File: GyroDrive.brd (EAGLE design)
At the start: 8.1 x 21 mm, 35 parts, among them Q1 TF412ST5G, Q2 TF412ST5G, Q3 TF412ST5G, Q4 TF412ST5G, Q5 TF412ST5G, Q6 TF412ST5G

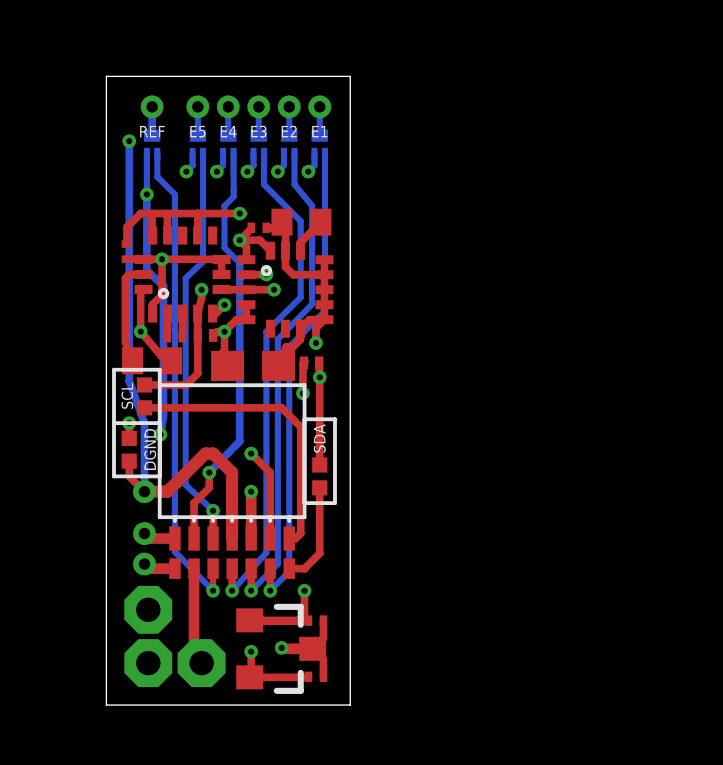
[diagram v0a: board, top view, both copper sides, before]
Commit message: Rev 2 submitted to Advanced Circuits for quote. Fixed spacing issues.
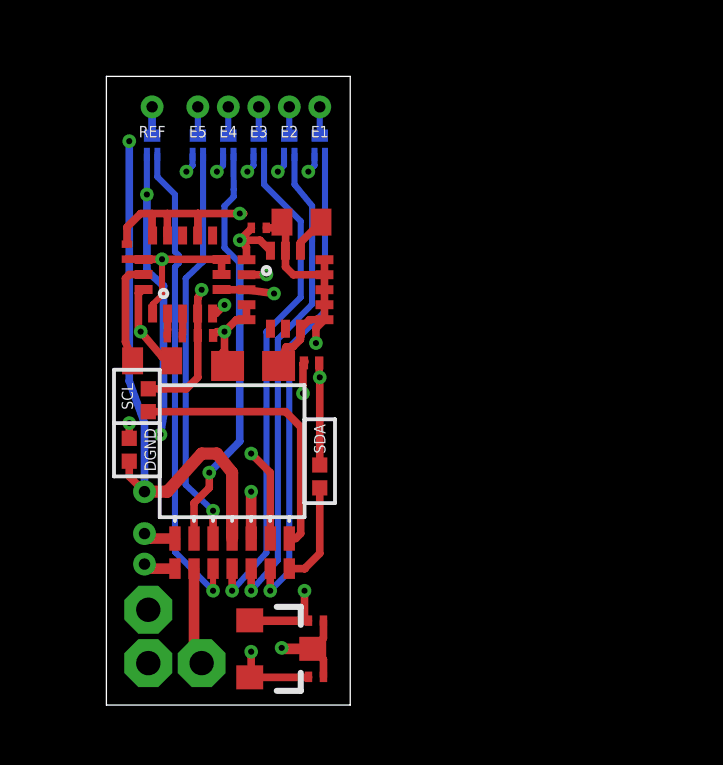
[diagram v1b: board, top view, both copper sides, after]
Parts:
- moved J_SCL 0.18 mm to (1.40, 10.2)

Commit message: Changed schematic to make more sense (Rev 3 to Advanced Circuits)
- Changed input voltage net name from +15V to VCC because VCC can be anything from 2.5V to 30V

- Separate nets for digital and analog grounds (DGND and GND)
-- Causes DRC to catch my mistake when digital and analog ground overlap

- New nets SDAOUT and SCLOUT to represent SDA and SCL after passing through jumper
-- Stops ratsnest from telling me I have things to do when the two terminals of the jumper are not connected to each other
-- Pullup resistors moved to SDA and SCL nets (they used to be near omnetics connector on schematic, which put them on SDAOUT and SCLOUT)

- Capacitors renumbered and moved around
-- Location on schematic is now more representative of location on the board
-- Numbered so that capacitors that are associated with the same IC are sequential.
--- C1-C2 for regulator
--- C3 for big bypass capacitor
--- C4-C5 for L3GD20H
--- C6-C8 for LSM303D
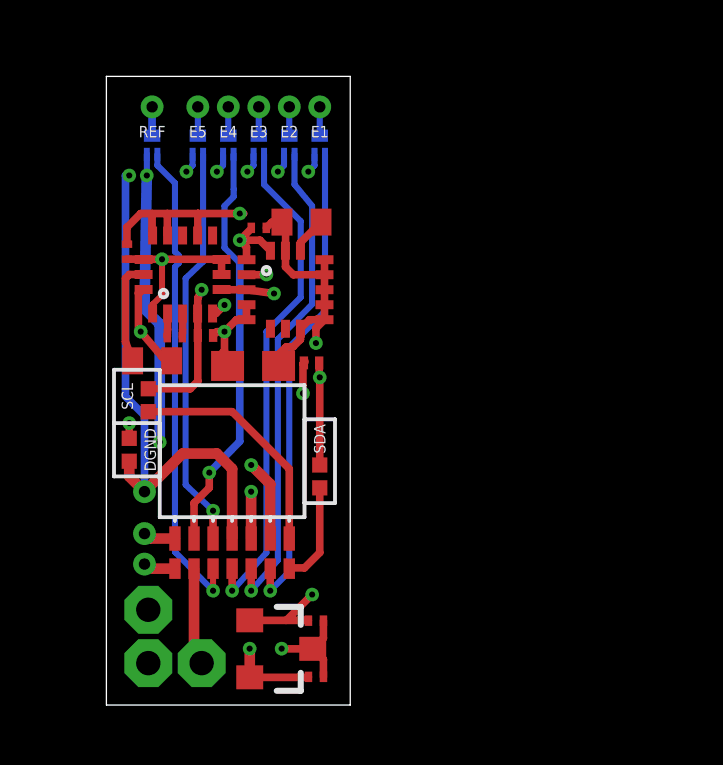
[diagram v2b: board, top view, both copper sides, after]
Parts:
- removed C9: 0.22 uF, resistor:C0201
- added C6: 0.1uF, resistor:C0201
- C3: value 0.1uF -> 10uF; device resistor:C0201 -> resistor:C0603
- C5: value 10uF -> 0.01 uF; device resistor:C0603 -> resistor:C0402
- C7: value 0.01 uF -> 0.22 uF; device resistor:C0402 -> resistor:C0201
- moved C7 5.70 mm to (2.28, 12.3)
- moved C3 5.67 mm to (4.89, 11.3), turned to 0 degrees
- moved C5 5.06 mm to (6.50, 16.1), turned to 180 degrees
- turned J_GND to 270 degrees
- turned J_SCL to 270 degrees
- turned J_SDA to 270 degrees
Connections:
- net +15V renamed VCC
- net N$11 renamed STIM1OUT
- net N$12 renamed ICOM
- net N$15 renamed IX
- net N$16 renamed STIM1IN
- new net DGND: C1.2, C2.2, C3.2, C4.2, C5.2, C6.2, C8.2, J_GND.1, U$1.P$10, U$1.P$11, U$1.P$12, U$1.P$13, U$1.P$15, U$1.P$8, U$1.P$9, U$2.3, U$3.P$10, U$3.P$12, U$3.P$13, U$3.P$16, U$3.P$5
- new net SCLOUT: J_SCL.2, U$10.K
- new net SDAOUT: J_SDA.2, U$10.P
- net +3V3: now also C6.1; no longer C5.1
- net GND: no longer C1.2, C2.2, C3.2, C4.2, C5.2, C7.2, C8.2, J_GND.1, U$1.P$10, U$1.P$11, U$1.P$12, U$1.P$13, U$1.P$15, U$1.P$8, U$1.P$9, U$2.3, U$3.P$10, U$3.P$12, U$3.P$13, U$3.P$16, U$3.P$5
- net N$2: now also C7.1; no longer C9.1
- net N$3: now also C7.2; no longer C9.2
- net N$9: now also C5.1; no longer C7.1
- net SCL: no longer J_SCL.2, U$10.K
- net SDA: no longer J_SDA.2, U$10.P
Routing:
- net GND: track 49.7 -> 23.0 mm, vias 7 -> 1
- net DGND: track 0.00 -> 24.8 mm, vias 0 -> 6
- net SCL: track 17.1 -> 7.74 mm
- net SCLOUT: track 0.00 -> 7.81 mm
- net SDA: track 13.8 -> 10.4 mm
- net SDAOUT: track 0.00 -> 3.40 mm
- net VCC: track 30.9 -> 30.3 mm
- net +3V3: track 25.4 -> 24.8 mm
- added copper zone on layer 3, net DGND

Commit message: WIP: reroute with no vias or traces under chip
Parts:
- moved C7 13.8 mm to (15.7, 9.21)
- moved U$3 13.8 mm to (16.0, 11.3)
- moved C6 13.6 mm to (14.0, 12.6)
- moved R1 13.0 mm to (15.7, 8.51), turned to 180 degrees
- moved C8 11.6 mm to (13.1, 12.0), turned to 90 degrees
- moved R2 11.3 mm to (17.8, 14.4)
- moved C5 11.3 mm to (17.7, 17.7), turned to 270 degrees
- moved C4 10.0 mm to (14.8, 18.6), turned to 90 degrees
- moved U$1 9.64 mm to (15.2, 16.5)
- moved C3 8.55 mm to (13.2, 9.33), turned to 90 degrees
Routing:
- net VCC: track 30.3 -> 0.00 mm, vias 9 -> 0
- net GND: track 23.0 -> 4.73 mm, vias 1 -> 0
- net S3: track 16.7 -> 0.00 mm, vias 1 -> 0
- net S2: track 16.3 -> 0.00 mm, vias 1 -> 0
- net VGND: track 16.2 -> 0.00 mm, vias 1 -> 0
- net S1: track 16.0 -> 0.00 mm, vias 1 -> 0
- net S4: track 13.8 -> 0.00 mm, vias 1 -> 0
- net S5: track 13.5 -> 0.00 mm, vias 1 -> 0
- net SCL: track 7.74 -> 18.1 mm, vias 2 -> 0
- net SCLOUT: track 7.81 -> 0.00 mm
- net SDA: track 10.4 -> 16.5 mm, vias 2 -> 0
- net +3V3: track 24.8 -> 18.9 mm, vias 5 -> 4
- net SDAOUT: track 3.40 -> 0.00 mm
- net DGND: track 24.8 -> 27.2 mm, vias 6 -> 3
- net N$1: track 3.45 -> 1.60 mm
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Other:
- board size 8.1 x 21 mm -> 8.3 x 21 mm

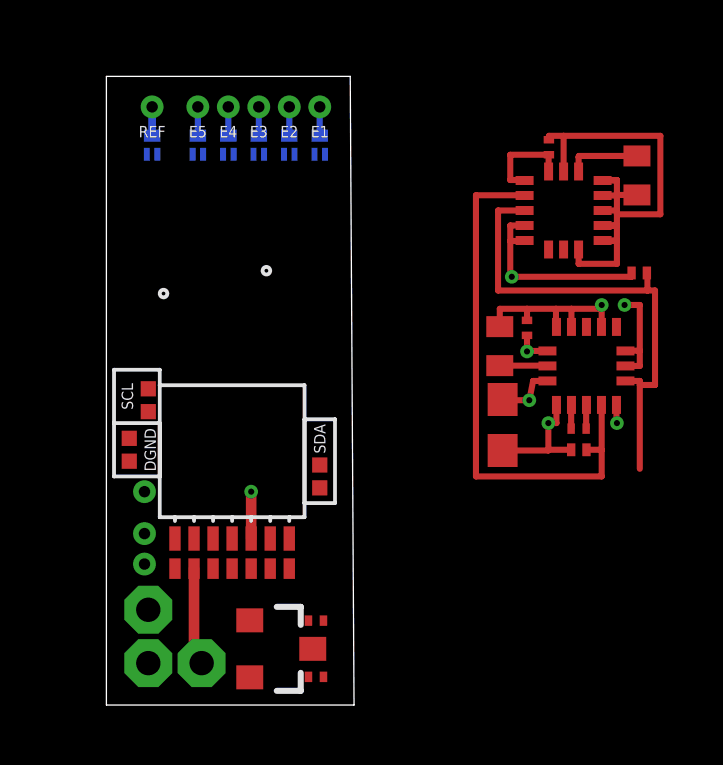
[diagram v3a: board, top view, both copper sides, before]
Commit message: Switched to Invensense MPU-9250
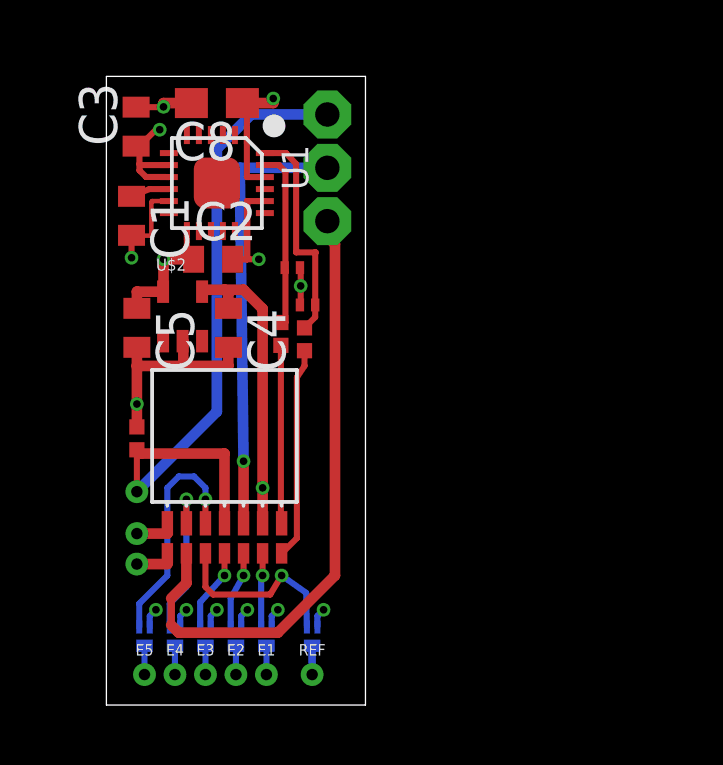
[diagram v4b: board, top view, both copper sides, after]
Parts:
- removed C6: 0.1uF, resistor:C0201
- removed C7: 0.22 uF, resistor:C0201
- removed U$1: L3GD20H, st:LGA16L
- removed U$3: LSM303D, st:LGA16L
- added U1: (no value), Grove - IMU 10DOF v1.1:LEAD-QFN24
- C1, C2: device resistor:C0201 -> resistor:C0402
- C3: value 10uF -> 10nF; device resistor:C0603 -> resistor:C0402
- C4: value 0.1uF -> (none); device resistor:C0201 -> resistor:C0402
- C5: value 0.01 uF -> (none)
- C8: value 4.7uF -> (none); device resistor:C0402 -> resistor:C0603
- U$2: value LM3480IM4 -> 2.5V; device SparkFun-PowerIC:SOT23-3 -> michael-stetner:SC70
- moved REF 19.7 mm to (6.86, 1.02), turned to 180 degrees
- moved E1 19.0 mm to (5.33, 1.02), turned to 180 degrees
- moved E2 19.0 mm to (4.32, 1.02), turned to 180 degrees
- moved E3 19.0 mm to (3.30, 1.02), turned to 180 degrees
- moved E4 19.0 mm to (2.29, 1.02), turned to 180 degrees
- moved E5 19.0 mm to (1.27, 1.02), turned to 180 degrees
- moved ICOM 17.6 mm to (7.37, 17.9)
- moved MOTORGND 17.6 mm to (7.37, 19.7)
- moved C5 17.4 mm to (1.02, 12.6)
- moved Q6 17.2 mm to (6.86, 2.29), turned to 270 degrees
- moved C1 16.6 mm to (0.84, 16.3), turned to 270 degrees
- moved Q1 16.5 mm to (5.33, 2.29), turned to 270 degrees
- moved Q2 16.5 mm to (4.32, 2.29), turned to 270 degrees
- moved Q3 16.5 mm to (3.30, 2.29), turned to 270 degrees
- moved Q4 16.5 mm to (2.29, 2.29), turned to 270 degrees
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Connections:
- removed net +3V3: C2.1, C3.1, C4.1, C6.1, R1.2, R2.2, U$1.P$1, U$1.P$16, U$1.P$4, U$1.P$5, U$2.1, U$3.P$1, U$3.P$14, U$3.P$7, U$3.P$8
- removed net N$1: C8.1, U$3.P$15
- removed net N$3: C7.2, U$3.P$2
- removed net N$9: C5.1, U$1.P$14
- new net VDD: C2.1, C3.1, C5.1, C8.1, R1.2, R2.2, U$2.5, U1.1, U1.13, U1.22, U1.8, U1.9
- net DGND: now also U$2.2, U1.11, U1.18, U1.20; no longer C6.2, U$1.P$10, U$1.P$11, U$1.P$12, U$1.P$13, U$1.P$15, U$1.P$8, U$1.P$9, U$2.3, U$3.P$10, U$3.P$12, U$3.P$13, U$3.P$16, U$3.P$5
- net N$2: now also C1.1, U1.10; no longer C7.1, U$3.P$3
- net SCL: now also U1.23; no longer U$1.P$2, U$3.P$4
- net SDA: now also U1.24; no longer U$1.P$3, U$3.P$6
- net VCC: now also C4.1, U$2.4; no longer C1.1, U$2.2
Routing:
- net +3V3: track 18.9 -> 0.00 mm, vias 4 -> 0
- net GND: track 4.73 -> 23.4 mm
- net IX: track 3.25 -> 20.9 mm
- net VCC: track 0.00 -> 15.3 mm, vias 0 -> 7
- net VDD: track 0.00 -> 14.8 mm, vias 0 -> 4
- net SCL: track 18.1 -> 6.09 mm
- net DGND: track 27.2 -> 18.1 mm, vias 3 -> 4
- net SDA: track 16.5 -> 7.47 mm
- net S5: track 0.00 -> 7.80 mm, vias 0 -> 1
- net SDAOUT: track 0.00 -> 7.04 mm
- net VGND: track 0.00 -> 6.27 mm, vias 0 -> 1
- net SCLOUT: track 0.00 -> 5.94 mm
- net S4: track 0.00 -> 5.29 mm, vias 0 -> 1
- net ICOM: track 9.81 -> 14.8 mm
- net S3: track 0.00 -> 2.77 mm, vias 0 -> 1
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- added copper zone on layer 15, net DGND
- added copper zone on layer 15, net GND
- added copper zone on layer 2, net VDD
- removed copper zone on layer 2, net +3V3
- removed copper zone on layer 3, net DGND
- removed copper zone on layer 3, net GND
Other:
- board size 8.3 x 21 mm -> 8.6 x 21 mm
- board text removed: "DGND"
- board text removed: "SCL"
- board text removed: "SDA"

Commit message: Moved motor solder points lower
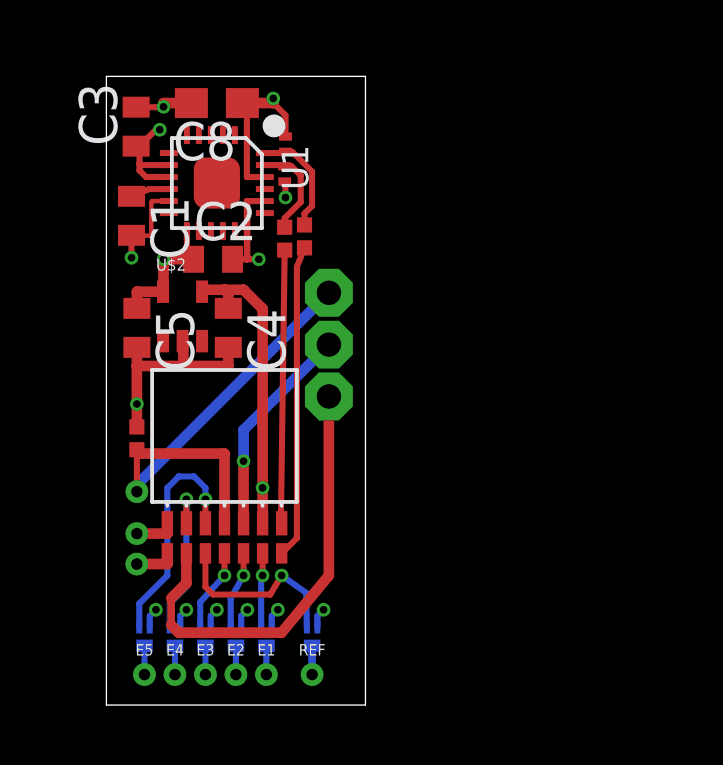
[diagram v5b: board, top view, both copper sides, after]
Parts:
- moved MOTORGND 5.94 mm to (7.42, 13.7)
- moved ICOM 5.89 mm to (7.42, 12.0)
- moved IX 5.84 mm to (7.42, 10.3)
- moved R2 5.41 mm to (5.97, 18.7), turned to 90 degrees
- moved J_SDA 3.43 mm to (6.60, 15.6)
- moved J_SCL 3.18 mm to (5.94, 15.5)
- moved R1 3.13 mm to (5.94, 17.7), turned to 270 degrees
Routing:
- net ICOM: track 14.8 -> 7.13 mm
- net GND: track 23.4 -> 16.0 mm
- net IX: track 20.9 -> 14.8 mm
- net SDA: track 7.47 -> 3.75 mm
- net SDAOUT: track 7.04 -> 10.4 mm
- net SCLOUT: track 5.94 -> 9.12 mm
- net SCL: track 6.09 -> 3.28 mm

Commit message: Added instrumentation amplifiers for neural signals
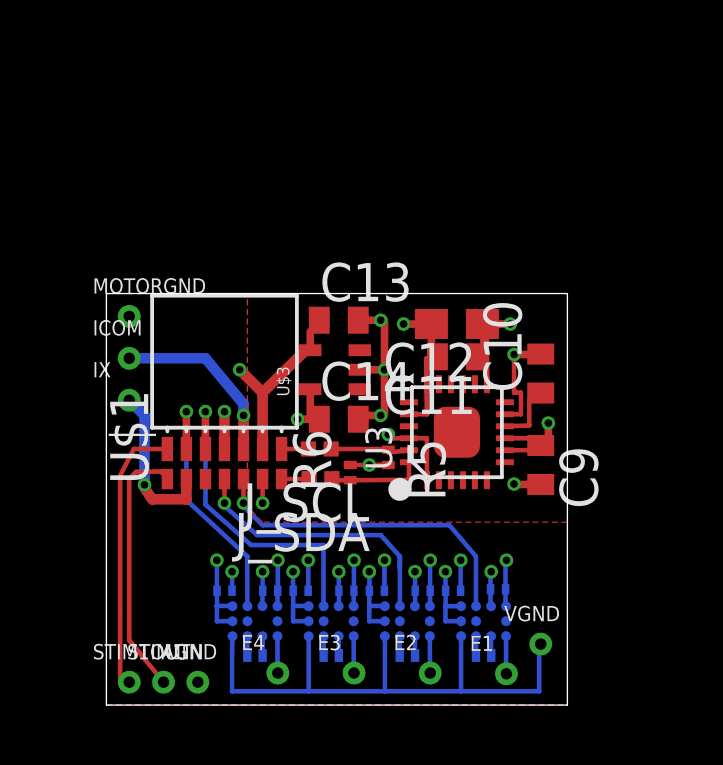
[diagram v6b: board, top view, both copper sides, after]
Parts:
- removed C1, C2: 0.1uF, resistor:C0402
- removed C3: 10nF, resistor:C0402
- removed C4, C5: (no value), resistor:C0402
- removed C8: (no value), resistor:C0603
- removed E5, GND, REF: (no value), michael-stetner:30MIL/15MIL
- removed J_GND: (no value), michael-stetner:SJ
- removed Q1, Q2, Q3, Q4, Q5, Q6: TF412ST5G, on-semiconductor-mes:SOT883
- removed R1, R2: 10k, resistor:R0201
- removed U$10: OMN-A75243-001, GFL:OMN-A75243-001
- removed U1: (no value), Grove - IMU 10DOF v1.1:LEAD-QFN24
- added AGND, VGND: (no value), michael-stetner:30MIL/15MIL
- added C10, C11: 0.1uF, resistor:C0402
- added C12: (no value), resistor:C0603
- added C13, C14: (no value), resistor:C0402
- added C15, C16, C17, C18, C19, C20, C21, C22: (no value), resistor:C0201
- added C9: 10nF, resistor:C0402
- added IC1, IC2, IC3, IC4: AD8235, analog-devices:BGA_CB11
- added R10, R7, R8, R9: (no value), resistor:R0201
- added R5, R6: 10k, resistor:R0201
- added U$1: OMN-A75243-001, GFL:OMN-A75243-001
- added U$3: 2.5V, michael-stetner:SC70
- added U3: (no value), Grove - IMU 10DOF v1.1:LEAD-QFN24
- ICOM, IX, MOTORGND: device wirepad:1,6/0,8 -> michael-stetner:30MIL/15MIL
- U$2: value 2.5V -> MICRODRIVE-MOTOR; device michael-stetner:SC70 -> michael-stetner:0206A001B-021-47:1-Y2825
- moved J_SDA 8.09 mm to (7.14, 7.54), turned to 180 degrees
- moved E1 8.00 mm to (13.3, 1.04), turned to 0 degrees
- moved J_SCL 7.11 mm to (7.11, 8.53), turned to 180 degrees
- moved MOTORGND 6.70 mm to (0.76, 13.0)
- moved ICOM 6.67 mm to (0.76, 11.6)
- moved IX 6.66 mm to (0.76, 10.2)
- moved E2 6.48 mm to (10.8, 1.07), turned to 0 degrees
- moved STIM1OUT 4.96 mm to (0.76, 0.76)
- moved E3 4.95 mm to (8.26, 1.07), turned to 0 degrees
- moved U$2 4.75 mm to (1.27, 17.5), flipped to the bottom, turned to 180 degrees
- moved STIM1IN 4.04 mm to (1.91, 0.76)
- moved E4 3.43 mm to (5.71, 1.07), turned to 0 degrees
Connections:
- removed net GND: GND.P$1, J_GND.2, MOTORGND.1, U$10.L
- removed net ICOM: ICOM.1, U$10.T
- removed net IX: IX.1, U$10.V
- removed net N$10: E1.P$1, Q1.P$3
- removed net N$2: C1.1, U1.10
- removed net N$4: Q6.P$3, REF.P$1
- removed net N$5: E5.P$1, Q5.P$3
- removed net N$6: E4.P$1, Q4.P$3
- removed net N$8: E2.P$1, Q2.P$3
- removed net S5: Q5.P$1, U$10.R
- removed net STIM1IN: STIM1IN.P$1, U$10.A
- removed net STIM1OUT: STIM1OUT.P$1, U$10.E
- removed net VCC: C4.1, Q1.P$2, Q2.P$2, Q3.P$2, Q4.P$2, Q5.P$2, Q6.P$2, U$10.U, U$2.4
- new net +VS: C13.1, C15.1, C17.1, C19.1, C21.1, IC1.A1, IC1.A2, IC2.A1, IC2.A2, IC3.A1, IC3.A2, IC4.A1, IC4.A2, U$1.U, U$3.4
- new net -VS: C16.1, C18.1, C20.1, C22.1, IC1.D1, IC2.D1, IC3.D1, IC4.D1, U$1.F
- new net AGND: AGND.P$1, C15.2, C16.2, C17.2, C18.2, C19.2, C20.2, C21.2, C22.2, IC1.C1, IC2.C1, IC3.C1, IC4.C1, MOTORGND.P$1, U$1.L
- new net E1: E1.P$1, IC1.D3
- new net E2: E2.P$1, IC2.D3
- new net E3: E3.P$1, IC3.D3
- new net E4: E4.P$1, IC4.D3
- new net N$14: IX.P$1, U$1.V
- new net N$15: STIM1IN.P$1, U$1.A
- new net N$16: STIM1OUT.P$1, U$1.E
- new net N$17: ICOM.P$1, U$1.T
- new net N$18: IC1.C3, R7.1
- new net N$19: IC1.B3, R7.2
- new net N$20: IC2.B3, R8.2
- new net N$21: IC2.C3, R8.1
- new net N$22: IC3.B3, R9.2
- new net N$23: IC3.C3, R9.1
- new net N$24: IC4.B3, R10.2
- new net N$25: IC4.C3, R10.1
- net DGND: now also C10.2, C11.2, C12.2, C13.2, C14.2, C9.2, U$1.D, U$3.2, U3.11, U3.18, U3.20; no longer C1.2, C2.2, C3.2, C4.2, C5.2, C8.2, J_GND.1, U$2.2, U1.11, U1.18, U1.20
- net N$7: now also C10.1, U3.10; no longer E3.P$1, Q3.P$3
- net S1: now also IC1.B1, U$1.B; no longer Q1.P$1, U$10.D
- net S2: now also IC2.B1, U$1.J; no longer Q2.P$1, U$10.B
- net S3: now also IC3.B1, U$1.R; no longer Q3.P$1, U$10.J
- net S4: now also IC4.B1, U$1.N; no longer Q4.P$1, U$10.N
- net SCL: now also R5.1, U3.23; no longer R1.1, U1.23
- net SCLOUT: now also U$1.K; no longer U$10.K
- net SDA: now also R6.1, U3.24; no longer R2.1, U1.24
- net SDAOUT: now also U$1.P; no longer U$10.P
- net VDD: now also C11.1, C12.1, C14.1, C9.1, R5.2, R6.2, U$3.5, U3.1, U3.13, U3.22, U3.8, U3.9; no longer C2.1, C3.1, C5.1, C8.1, R1.2, R2.2, U$2.5, U1.1, U1.13, U1.22, U1.8, U1.9
- net VGND: now also IC1.A3, IC2.A3, IC3.A3, IC4.A3, VGND.P$1; no longer Q6.P$1, U$10.F
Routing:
- net +VS: track 0.00 -> 18.7 mm, vias 0 -> 5
- net GND: track 16.0 -> 0.00 mm
- net VCC: track 15.3 -> 0.00 mm, vias 7 -> 0
- net IX: track 14.8 -> 0.00 mm
- net VGND: track 6.27 -> 19.2 mm, vias 1 -> 0
- net AGND: track 0.00 -> 11.6 mm, vias 0 -> 9
- net SDAOUT: track 10.4 -> 0.93 mm
- net N$16: track 0.00 -> 9.31 mm
- net N$15: track 0.00 -> 8.67 mm
- net S1: track 2.51 -> 11.1 mm
- net SCLOUT: track 9.12 -> 0.89 mm
- net S3: track 2.77 -> 10.8 mm
- net S5: track 7.80 -> 0.00 mm, vias 1 -> 0
- net ICOM: track 7.13 -> 0.00 mm, vias 1 -> 0
- net S2: track 2.57 -> 9.47 mm
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- added copper zone on layer 2, net +VS
- added copper zone on layer 1, net -VS
- added copper zone on layer 15, net AGND
- removed copper zone on layer 15, net GND
- removed copper zone on layer 2, net VCC
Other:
- board size 8.6 x 21 mm -> 15.4 x 13.7 mm
- board text removed: "Michael Stetner Fee Lab 2015"
- board text removed: "X"
- board text removed: "Y"
- board text removed: "Z"
